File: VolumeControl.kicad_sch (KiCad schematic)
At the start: 44 parts, among them J1 Conn_01x03, J2 Conn_01x03, U6 NE5532, U7 NE5532, U8 NE5532, U9 NE5532

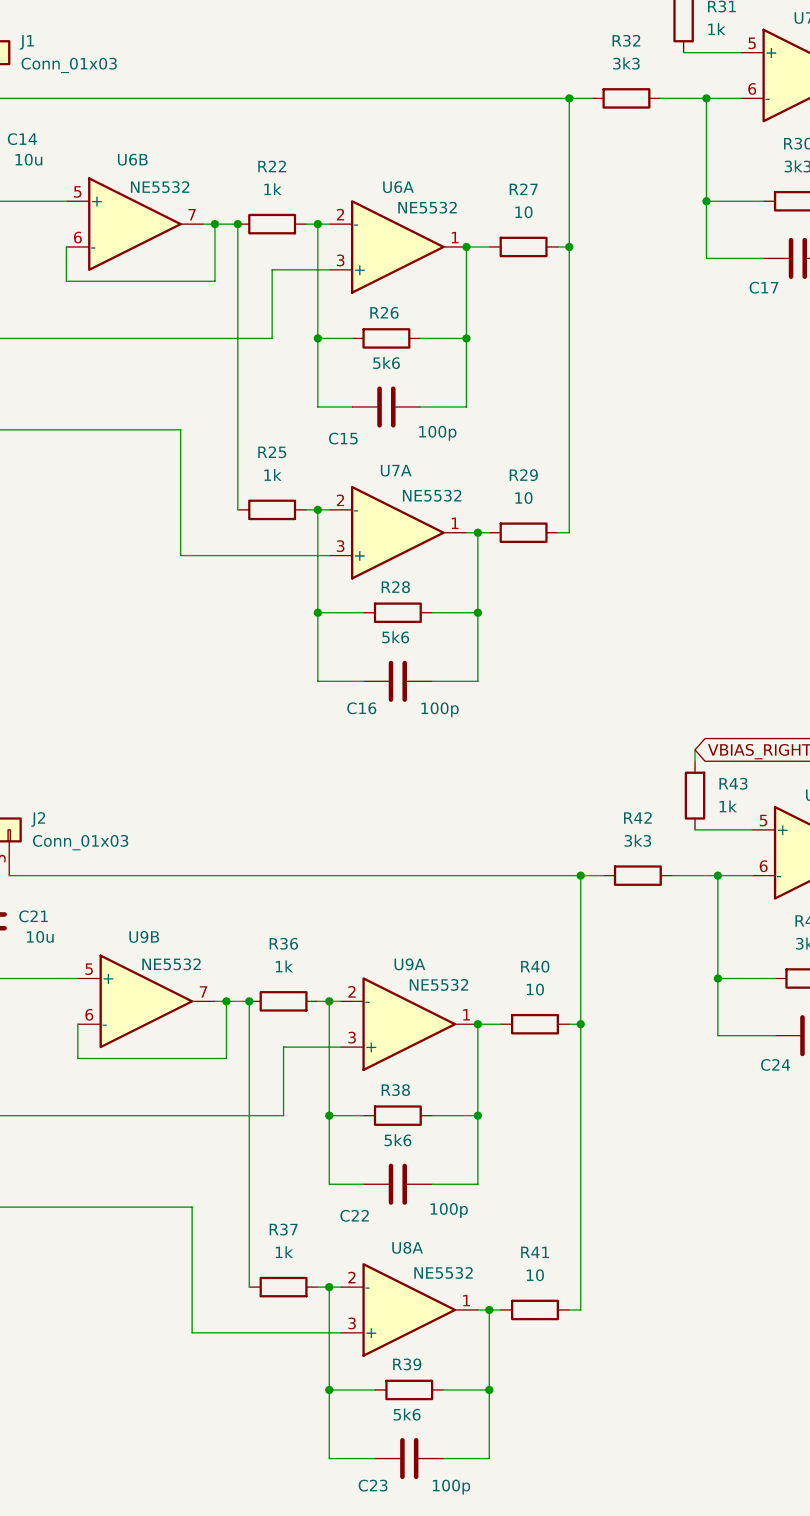
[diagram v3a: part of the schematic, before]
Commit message: Add inputs audio and power and correct errors
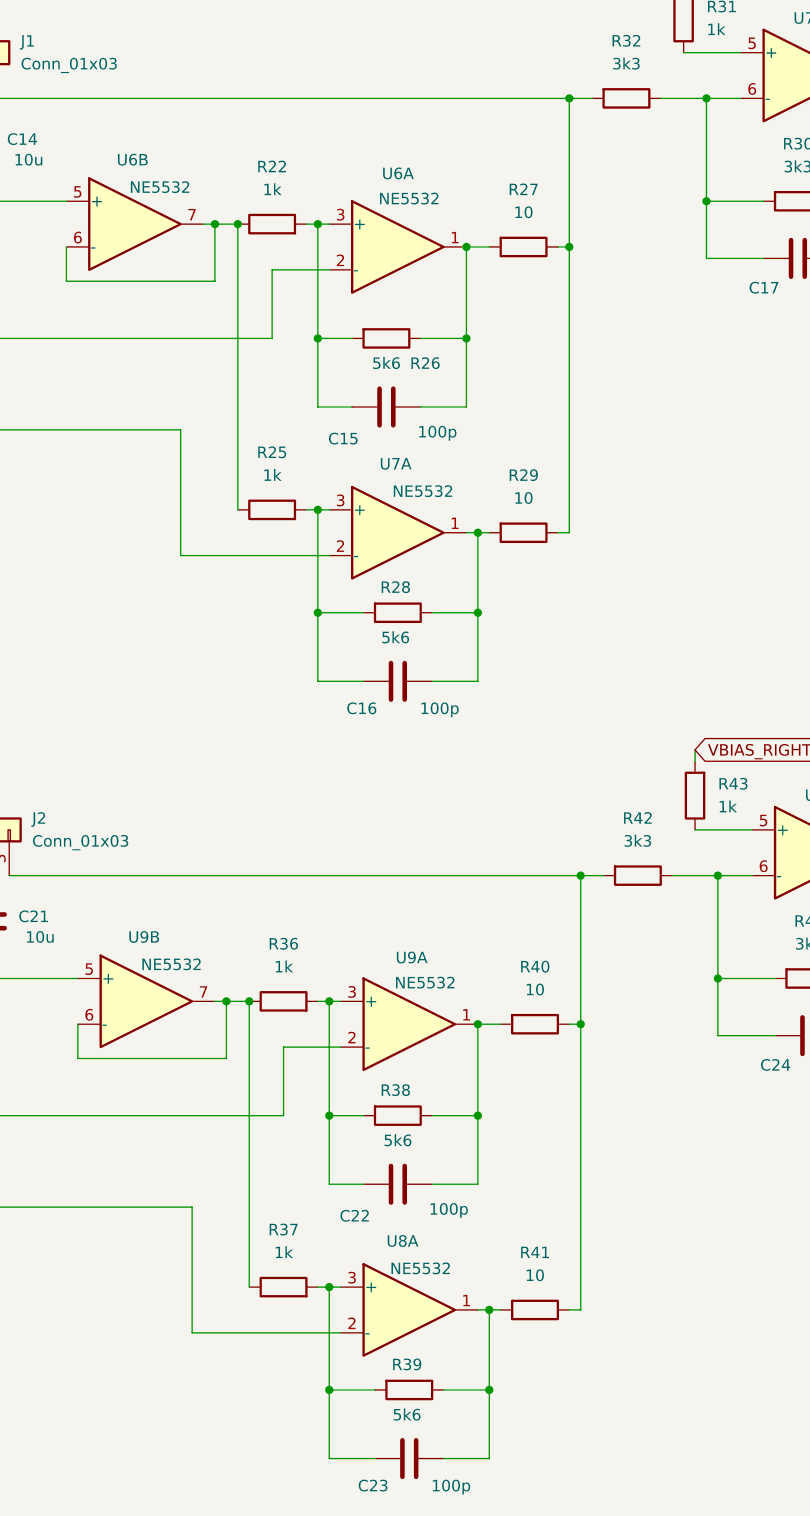
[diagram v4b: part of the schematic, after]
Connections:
- net at C16.1, R25.2, R28.2: now also U7.3 (+); no longer U7.2 (-)
- net at C22.1, R36.2, R38.2: now also U9.3 (+); no longer U9.2 (-)
- net at C15.1, R22.2, R26.2: now also U6.3 (+); no longer U6.2 (-)
- net at R23.1: now also U7.2 (-); no longer U7.3 (+)
- net at R34.1: now also U9.2 (-); no longer U9.3 (+)
- net at C23.1, R37.2, R39.2: now also U8.3 (+); no longer U8.2 (-)
- net at R35.1: now also U8.2 (-); no longer U8.3 (+)
- net at R24.1: now also U6.2 (-); no longer U6.3 (+)
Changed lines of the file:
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@@
 	)
 	(junction
+		(at 116.84 144.78)
+		(diameter 0)
+		(color 0 0 0 0)
+	)
+	(junction
 		(at 127 41.91)
 		(diameter 0)
@@
 	)
 	(junction
-		(at 116.84 144.78)
-		(diameter 0)
-		(color 0 0 0 0)
-	)
-	(junction
 		(at 238.76 144.78)
 		(diameter 0)
@@
 	)
 	(symbol
-		(lib_name "NE5532_1")
 		(lib_id "Amplifier_Operational:NE5532")
 		(at 240.03 53.34 0)
@@
 	)
 	(symbol
-		(lib_name "NE5532_2")
 		(lib_id "Amplifier_Operational:NE5532")
-		(at 107.95 96.52 0)
+		(at 107.95 90.17 0)
 		(unit 1)
 		(exclude_from_sim no)
@@
 		(dnp no)
 		(property "Reference" "U7"
-			(at 107.696 83.312 0)
+			(at 107.696 82.55 0)
 			(effects
 				(font
@@
 		)
 		(property "Value" "NE5532"
-			(at 111.76 86.106 0)
+			(at 110.744 85.598 0)
 			(effects
 				(font
@@
 		)
 		(property "Footprint" "Package_SO:SOIC-8_3.9x4.9mm_P1.27mm"
-			(at 107.95 96.52 0)
+			(at 107.95 90.17 0)
 			(effects
 				(font
@@
 		)
 		(property "Datasheet" "http://www.ti.com/lit/ds/symlink/ne5532.pdf"
-			(at 107.95 96.52 0)
+			(at 107.95 90.17 0)
 			(effects
 				(font
@@
 		)
 		(property "Description" "Dual Low-Noise Operational Amplifiers, DIP-8/SOIC-8"
-			(at 107.95 96.52 0)
+			(at 107.95 90.17 0)
 			(effects
 				(font
@@
 	)
 	(symbol
-		(lib_name "NE5532_2")
 		(lib_id "Amplifier_Operational:NE5532")
-		(at 109.22 151.13 0)
+		(at 109.22 144.78 0)
 		(unit 1)
 		(exclude_from_sim no)
@@
 		(dnp no)
 		(property "Reference" "U9"
-			(at 109.22 138.176 0)
+			(at 109.474 137.414 0)
 			(effects
 				(font
@@
 		)
 		(property "Value" "NE5532"
-			(at 112.522 140.462 0)
+			(at 110.998 140.208 0)
 			(effects
 				(font
@@
 		)
 		(property "Footprint" "Package_SO:SOIC-8_3.9x4.9mm_P1.27mm"
-			(at 109.22 151.13 0)
+			(at 109.22 144.78 0)
 			(effects
 				(font
@@
 		)
 		(property "Datasheet" "http://www.ti.com/lit/ds/symlink/ne5532.pdf"
-			(at 109.22 151.13 0)
+			(at 109.22 144.78 0)
 			(effects
 				(font
@@
 		)
 		(property "Description" "Dual Low-Noise Operational Amplifiers, DIP-8/SOIC-8"
-			(at 109.22 151.13 0)
+			(at 109.22 144.78 0)
 			(effects
 				(font
@@
 	)
 	(symbol
-		(lib_name "NE5532_2")
 		(lib_id "Amplifier_Operational:NE5532")
-		(at 109.22 182.88 0)
+		(at 109.22 176.53 0)
 		(unit 1)
 		(exclude_from_sim no)
@@
 		(dnp no)
 		(property "Reference" "U8"
-			(at 108.966 169.672 0)
+			(at 108.458 168.91 0)
 			(effects
 				(font
@@
 		)
 		(property "Value" "NE5532"
-			(at 113.03 172.466 0)
+			(at 110.49 171.958 0)
 			(effects
 				(font
@@
 		)
 		(property "Footprint" "Package_SO:SOIC-8_3.9x4.9mm_P1.27mm"
-			(at 109.22 182.88 0)
+			(at 109.22 176.53 0)
 			(effects
 				(font
@@
 		)
 		(property "Datasheet" "http://www.ti.com/lit/ds/symlink/ne5532.pdf"
-			(at 109.22 182.88 0)
+			(at 109.22 176.53 0)
 			(effects
 				(font
@@
 		)
 		(property "Description" "Dual Low-Noise Operational Amplifiers, DIP-8/SOIC-8"
-			(at 109.22 182.88 0)
+			(at 109.22 176.53 0)
 			(effects
 				(font
@@
 	)
 	(symbol
-		(lib_name "NE5532_3")
 		(lib_id "Amplifier_Operational:NE5532")
 		(at 78.74 55.88 0)
@@
 	)
 	(symbol
-		(lib_name "NE5532_3")
 		(lib_id "Amplifier_Operational:NE5532")
 		(at 80.01 142.24 0)
@@
 	)
 	(symbol
-		(lib_name "NE5532_2")
 		(lib_id "Amplifier_Operational:NE5532")
-		(at 107.95 64.77 0)
+		(at 107.95 58.42 0)
 		(unit 1)
 		(exclude_from_sim no)
@@
 		(dnp no)
 		(property "Reference" "U6"
-			(at 107.95 51.816 0)
+			(at 107.95 50.292 0)
 			(effects
 				(font
@@
 		)
 		(property "Value" "NE5532"
-			(at 111.252 54.102 0)
+			(at 109.22 53.086 0)
 			(effects
 				(font
@@
 		)
 		(property "Footprint" "Package_SO:SOIC-8_3.9x4.9mm_P1.27mm"
-			(at 107.95 64.77 0)
+			(at 107.95 58.42 0)
 			(effects
 				(font
@@
 		)
 		(property "Datasheet" "http://www.ti.com/lit/ds/symlink/ne5532.pdf"
-			(at 107.95 64.77 0)
+			(at 107.95 58.42 0)
 			(effects
 				(font
@@
 		)
 		(property "Description" "Dual Low-Noise Operational Amplifiers, DIP-8/SOIC-8"
-			(at 107.95 64.77 0)
+			(at 107.95 58.42 0)
 			(effects
 				(font
@@
 	)
 	(symbol
-		(lib_name "NE5532_1")
 		(lib_id "Amplifier_Operational:NE5532")
 		(at 241.3 133.35 0)
@@
 		(dnp no)
 		(property "Reference" "R26"
-			(at 106.426 65.786 90)
+			(at 110.998 71.374 90)
 			(effects
 				(font
